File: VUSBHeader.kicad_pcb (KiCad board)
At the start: 2 copper layers, 16.6 x 20.2 mm, 12 parts, among them J1 USB_B_Micro, J3 Conn_01x02_Pin, J4 Conn_01x06_Pin

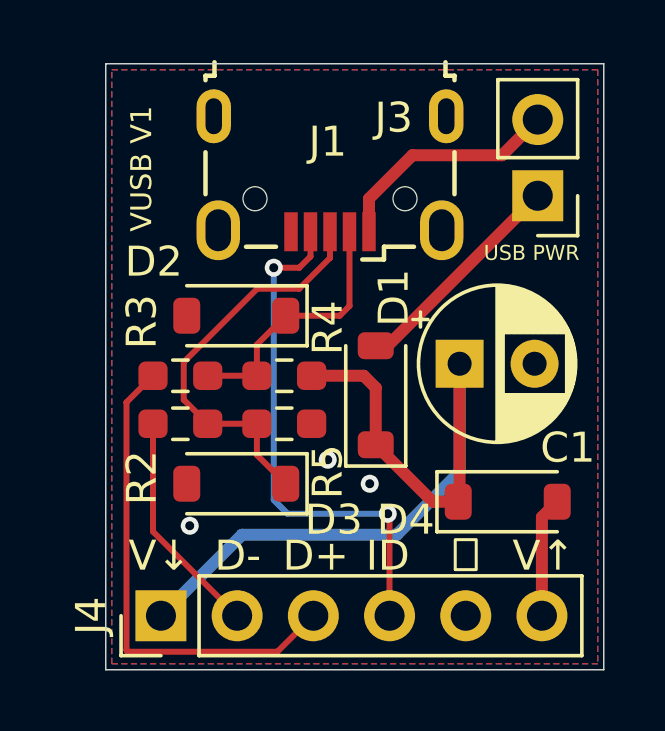
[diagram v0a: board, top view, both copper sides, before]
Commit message: Fix D- and D+ labeling
The D- and D+ labels were swapped on the board, so correct them. Also
update the README and move the manufacturing notes to make them easier
to read
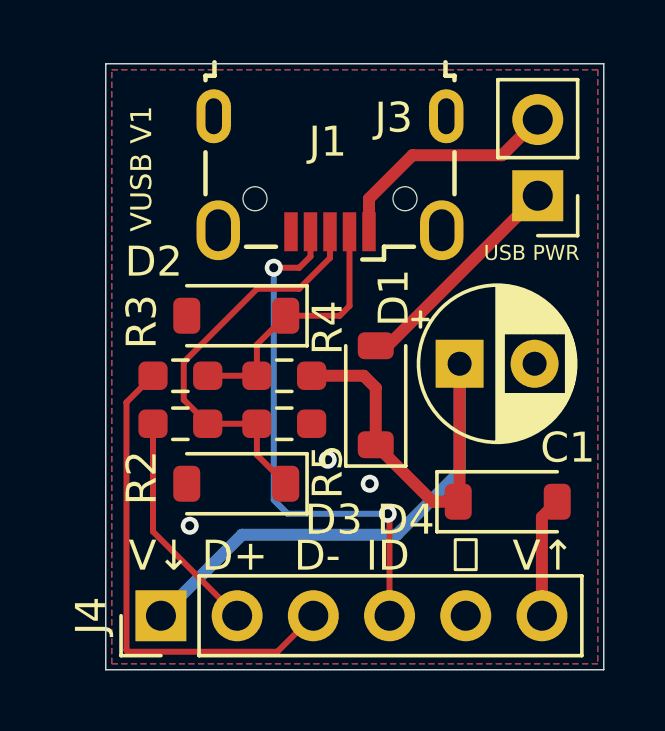
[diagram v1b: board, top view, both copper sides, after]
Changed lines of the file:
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@@
 		)
 		(fp_text user "${REFERENCE}"
-			(at 0 6.35 360)
+			(at 0 6.35 0)
 			(layer "F.Fab")
 			(effects
@@
 		(tags "usb micro receptacle")
 		(property "Reference" "J1"
-			(at 0.075 1.1 360)
+			(at 0.075 1.1 0)
 			(layer "F.SilkS")
 			(effects
@@
 		)
 		(property "Value" "USB_B_Micro"
-			(at 0 5.6 360)
+			(at 0 5.6 0)
 			(layer "F.Fab")
 			(effects
@@
 		)
 		(fp_text user "PCB Edge"
-			(at 0 3.75 360)
+			(at 0 3.75 0)
 			(layer "Dwgs.User")
 			(effects
@@
 		)
 		(fp_text user "${REFERENCE}"
-			(at 0 1.05 360)
+			(at 0 1.05 0)
 			(layer "F.Fab")
 			(effects
@@
 		(tags "SOD-123")
 		(property "Reference" "D3"
-			(at -3.25 -1.2 360)
+			(at -3.25 -1.2 0)
 			(layer "F.SilkS")
 			(effects
@@
 		)
 		(property "Value" "3.6V"
-			(at 0 2.1 360)
+			(at 0 -1.8 0)
 			(layer "F.Fab")
 			(effects
@@
 		)
 		(fp_text user "${REFERENCE}"
-			(at -3.25 -1.2 360)
+			(at -3.25 -1.2 0)
 			(layer "F.Fab")
 			(effects
@@
 		)
 		(property "Value" "1.5K"
-			(at 0 1.43 0)
+			(at 1.6 -2.35 90)
 			(layer "F.Fab")
 			(effects
@@
 		)
 		(property "Value" "1M"
-			(at 0 1.43 360)
+			(at -1.35 -1.8 90)
 			(layer "F.Fab")
 			(effects
@@
 		)
 		(fp_text user "${REFERENCE}"
-			(at 0 0 360)
+			(at 0 0 0)
 			(layer "F.Fab")
 			(effects
@@
 		)
 		(property "Value" "D_Schottky"
-			(at 0 2.1 90)
+			(at 3.25 3.05 180)
 			(layer "F.Fab")
 			(effects
@@
 		)
 		(property "Value" "68"
-			(at 0 1.43 360)
+			(at -2.6875 0.05 0)
 			(layer "F.Fab")
 			(effects
@@
 		)
 		(fp_text user "${REFERENCE}"
-			(at 0 0 360)
+			(at 0 0 0)
 			(layer "F.Fab")
 			(effects
@@
 		(tags "SOD-123")
 		(property "Reference" "D2"
-			(at 2.75 1.8 360)
+			(at 2.75 1.8 0)
 			(layer "F.SilkS")
 			(effects
@@
 		)
 		(property "Value" "3.6V"
-			(at 0 2.1 360)
+			(at 3.3 0.6 0)
 			(layer "F.Fab")
 			(effects
@@
 		)
 		(fp_text user "${REFERENCE}"
-			(at 1.75 1.8 360)
+			(at 2.8 1.8 0)
 			(layer "F.Fab")
 			(effects
@@
 		(tags "Through hole pin header THT 1x02 2.54mm single row")
 		(property "Reference" "J3"
-			(at 4.8 2.6 360)
+			(at 4.8 2.6 0)
 			(layer "F.SilkS")
 			(effects
@@
 		)
 		(property "Value" "Conn_01x02_Pin"
-			(at 0 4.87 360)
+			(at 0 4.87 0)
 			(layer "F.Fab")
 			(effects
@@
 		)
 		(property "Value" "68"
-			(at 0 1.43 360)
+			(at -2.6875 0.15 0)
 			(layer "F.Fab")
 			(effects
@@
 		)
 		(fp_text user "${REFERENCE}"
-			(at 0 0 360)
+			(at 0 0 0)
 			(layer "F.Fab")
 			(effects
@@
 		)
 		(property "Value" "4.7uF"
-			(at 1.25 3.75 0)
+			(at 1.25 2.8 0)
 			(layer "F.Fab")
 			(effects
@@
 	)
 	(gr_text "D+"
-		(at 128.2 88.6 0)
+		(at 125.5 88.6 0)
 		(layer "F.SilkS")
 		(effects
@@
 	)
 	(gr_text "D-"
-		(at 125.6 88.6 0)
+		(at 128.25 88.6 0)
 		(layer "F.SilkS")
 		(effects
@@
 	)
 	(zone
+		(net 0)
+		(net_name "")
+		(layer "F.Cu")
+		(hatch edge 0.5)
+		(connect_pads
+			(clearance 0)
+		)
+		(min_thickness 0.25)
+		(filled_areas_thickness no)
+		(keepout
+			(tracks allowed)
+			(vias allowed)
+			(pads allowed)
+			(copperpour not_allowed)
+			(footprints allowed)
+		)
+		(fill
+			(thermal_gap 0.5)
+			(thermal_bridge_width 0.5)
+		)
+		(polygon
+			(pts
+				(xy 127 75.5) (xy 130.5 75.5) (xy 130.5 77) (xy 127 77)
+			)
+		)
+	)
+	(zone
